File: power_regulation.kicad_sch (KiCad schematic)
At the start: 52 parts, among them J2 Conn_01x02, J3 Conn_02x01, U2 LM3880-1AA, U3 LMR33630BDDA, U4 LMR33630BDDA, U5 TPS78533QKVURQ1, U6 TPS78450QDBVRQ1

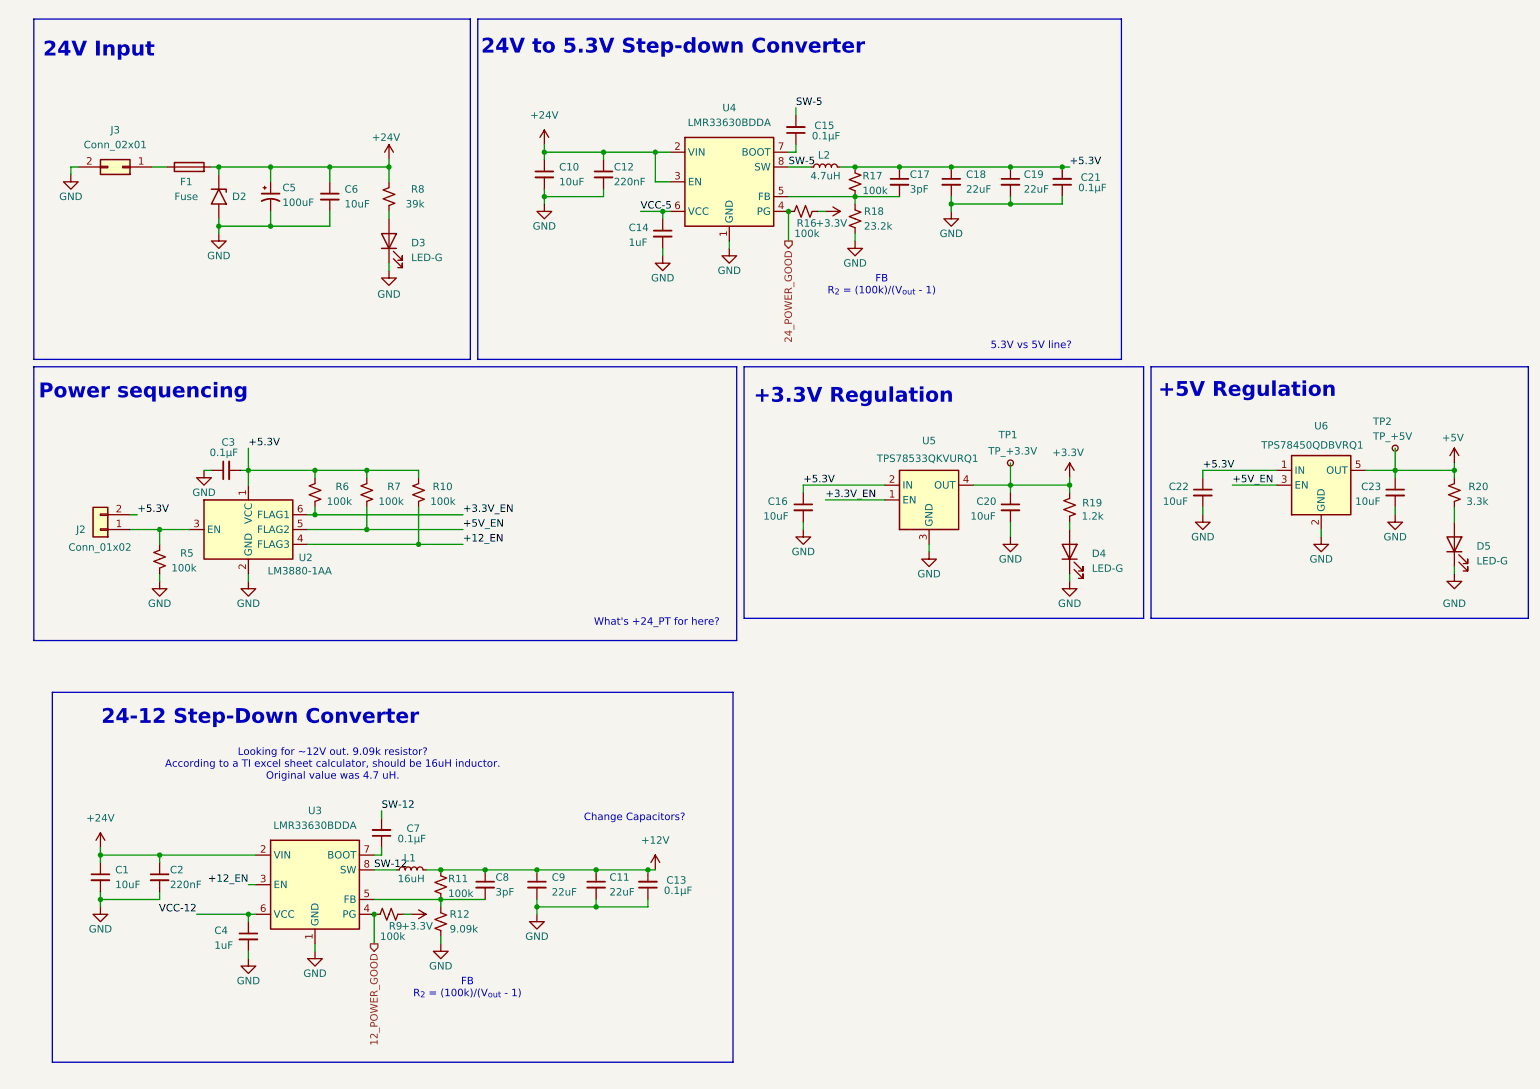
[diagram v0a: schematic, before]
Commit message: update buck converter components and add reverse polarity protection
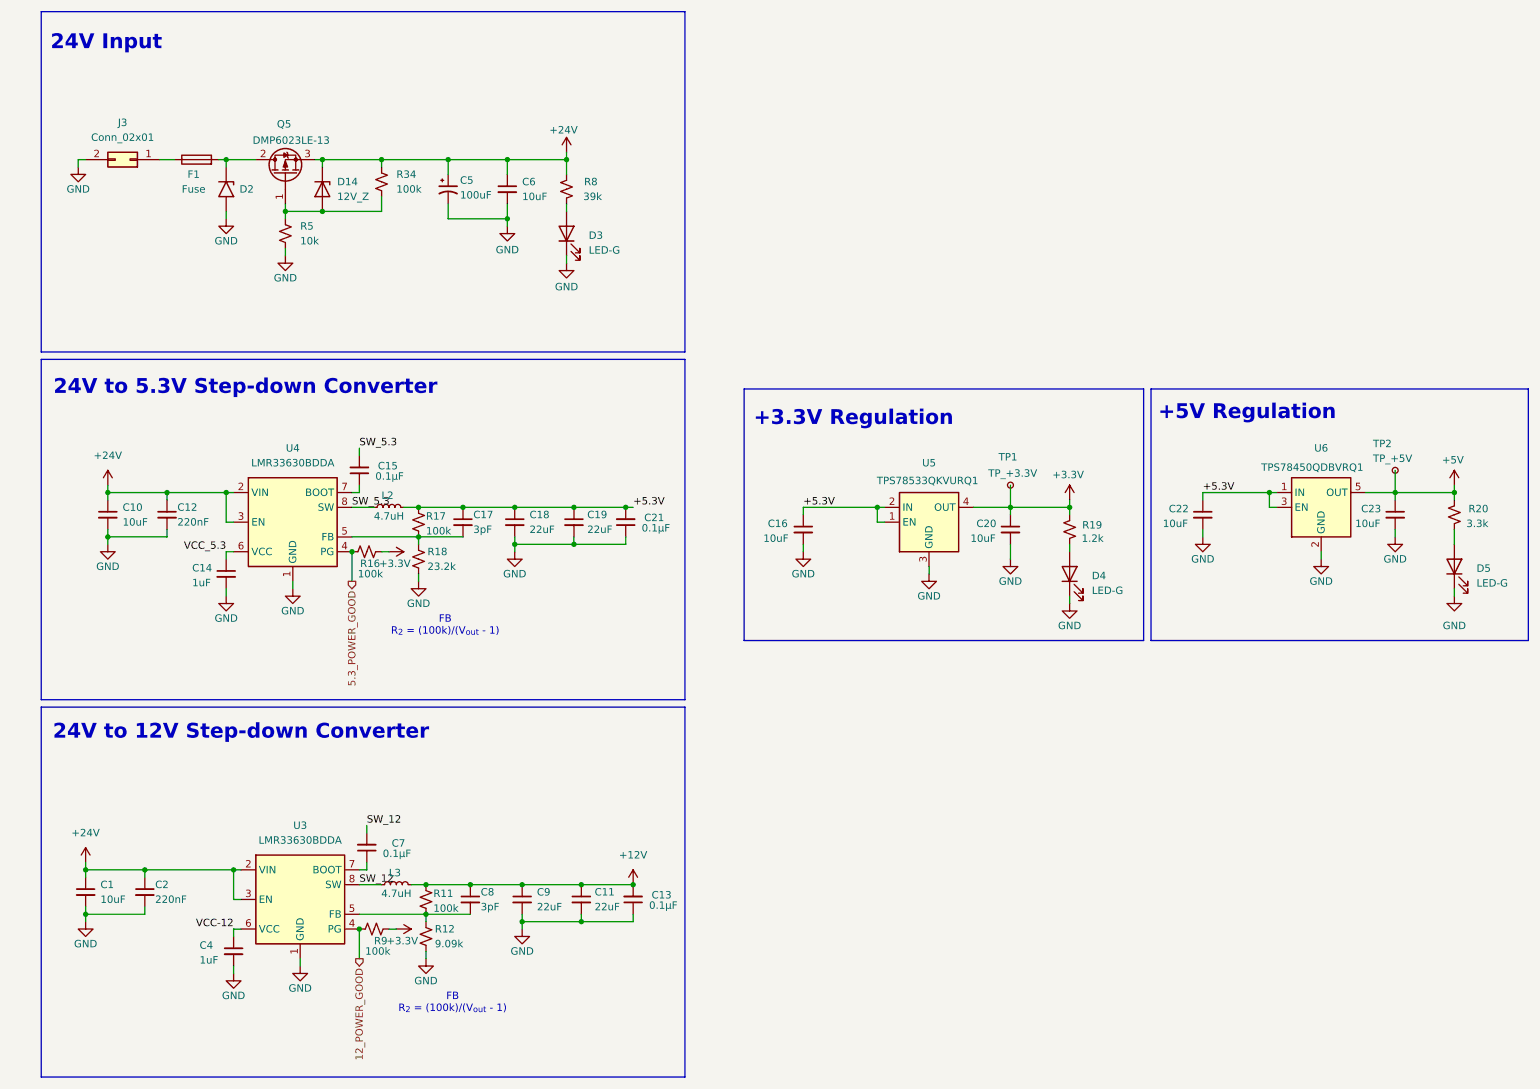
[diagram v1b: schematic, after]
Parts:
- removed C3: 0.1μF, Capacitor_SMD:C_0402_1005Metric, symbol Device:C_Small
- removed J2: Conn_01x02, Connector_Molex:Molex_Micro-Fit_3.0_43650-0215_1x02_P3.00mm_Vertical, symbol Connector_Generic:Conn_01x02
- removed L1: 16uH, Inductor_SMD:L_Bourns_SRP7028A_7.3x6.6mm, symbol Device:L_Small
- removed R10, R6, R7: 100k, Resistor_SMD:R_0603_1608Metric, symbol Device:R_Small_US
- removed U2: LM3880-1AA, Package_TO_SOT_SMD:SOT-23-6, symbol Power_Supervisor:LM3880
- added D14: 12V_Z, Diode_SMD:D_SOD-123, symbol Device:D_Zener
- added L3: 4.7uH, Inductor_SMD:L_Bourns_SRP7028A_7.3x6.6mm, symbol Device:L_Small
- added Q5: DMP6023LE-13, Package_TO_SOT_SMD:SOT-223-3_TabPin2, symbol Transistor_FET:ZXMP4A16G
- added R34: 100k, Resistor_SMD:R_0603_1608Metric, symbol Device:R_Small_US
- R12, R18: LCSC C25890 -> (none)
- R5: value 100k -> 10k
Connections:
- net +12_EN is gone; now on net +24V: U3.3 (EN)
- net +3.3V_EN is gone; now on net +5.3V: U5.1 (EN)
- net +5V_EN is gone; now on net +5.3V: U6.3 (EN)
- net +12V: now also L3.2
- net +24V: now also D14.1 (K), Q5.3 (S), R34.1; no longer D2.1 (A1), F1.2
- net GND: now also R5.2; no longer R5.1
- net 24_POWER_GOOD renamed 5.3_POWER_GOOD
- net SW-12 renamed SW_12
- net SW_12: now also L3.1
- net SW-5 renamed SW_5.3
- net VCC-5 renamed VCC_5.3
- new net: D14.2 (A), Q5.1 (G), R34.2, R5.1
- new net: D2.1 (A1), F1.2, Q5.2 (D)
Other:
- note added: "24V to 12V Step-down Converter"
- note removed: "24-12 Step-Down Converter"
- note removed: "5.3V vs 5V line?"
- note removed: "Change Capacitors?"
- note removed: "Looking for ~12V out. 9.09k resistor? According to a TI excel sheet calculator, should be 16uH inductor. Original value was 4.7 uH."
- note removed: "Power sequencing"
- note removed: "What's +24_PT for here?"
- moved on the sheet: C1, C10, C11, C12, C13, C14, C15, C16, C17, C18, C19, C2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

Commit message: do some pcb routing
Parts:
- renumbered C12 to C10, C14 to C11, C4 to C12, C15 to C13, C7 to C14, C5 to C15, C17 to C16, C8 to C17, C6 to C18, C18 to C19, C9 to C20, C19 to C21, C11 to C22, C21 to C23, C13 to C24, C16 to C25, C20 to C26, C22 to C27, C23 to C28, C1 to C7, C10 to C8, C2 to C9, D2 to D5, D14 to D6, D3 to D7, D4 to D8, D5 to D9, J3 to J4, L2 to L1, L3 to L2, Q5 to Q1, R16 to R10, R9 to R11, R34 to R12, R17 to R13, R18 to R14, R11 to R15, R12 to R16, R8 to R17, R19 to R18, R20 to R19, R5 to R9, TP1 to TP3, TP2 to TP4, U4 to U2, U5 to U4, U6 to U5
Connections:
- net VCC-12 renamed VCC_12
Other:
- moved on the sheet: C12, C14, C17, C20, C22, C24, C7, C9, L2, R11, R15, R16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

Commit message: finish pcb routing
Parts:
- added C34, C35, C36: 0.1μF, Capacitor_SMD:C_0402_1005Metric, symbol Device:C_Small
- added TP5: GND_TP, TestPoint:TestPoint_Loop_D2.50mm_Drill1.0mm, symbol Connector:TestPoint
- added TP6: 24V_TP, TestPoint:TestPoint_Loop_D2.50mm_Drill1.0mm, symbol Connector:TestPoint
- added U7: LM66200DRLR, Package_TO_SOT_SMD:SOT-583-8, symbol LM66200DRLR:LM66200DRLR
- R14: value 23.2k -> 24k
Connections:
- net +24V: now also TP6.1
- net GND: now also C34.1, C35.1, C36.1, TP5.1, U7.1 (GND), U7.4 (~{ON}), U7.5 (GND)
- net +5.3V renamed +5.17V
- net +5.17V: now also C36.2, U7.2 (VOUT), U7.7 (VOUT); no longer C16.1, C19.1, C21.1, C23.2, L1.2, R13.1
- net 5.3_POWER_GOOD renamed 5.17_POWER_GOOD
- new net +5.17V_PRE: C16.1, C19.1, C21.1, C23.2, C34.2, L1.2, R13.1, U7.3 (VIN1)
- new net 5V_USB: C35.2, U7.6 (VIN2)
- no-connect marks 0 -> 1
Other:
- note added: "24V to 5.17V Step-down Converter"
- note added: "USB ORing"
- note added: "Use buck to drop just above 5V so that ripple can be smoothed by 5V LDO"
- note removed: "24V to 5.3V Step-down Converter"

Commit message: remove unneccesary component fields
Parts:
- C10, C9: Dielectric X5R or X7R -> (none); LCSC C5378 -> (none); Voltage 50V -> (none)
- C11, C12: Dielectric X5R or X7R -> (none); LCSC C29936 -> (none)
- C13, C14, C23, C24, C34, C35, C36: value 0.1μF -> 100nF; LCSC C307331 -> (none); MPN CL05B104KO5NNNC -> (none)
- C16, C17: Dielectric X5R or X7R -> (none); LCSC C695157 -> (none)
- C18: footprint Capacitor_SMD:C_1812_4532Metric -> Capacitor_SMD:C_1206_3216Metric; Dielectric X5R or X7R -> (none); P/N CL31A106KBHNNNE -> (none); Voltage 50V -> (none)
- C19, C20, C21, C22: Dielectric X5R or X7R -> (none); LCSC C602037 -> (none)
- C25, C26, C27, C28: Dielectric X5R or X7R -> (none); LCSC C15850 -> (none)
- C7, C8: Dielectric X5R or X7R -> (none); LCSC C13585 -> (none); P/N CL31A106KBHNNNE -> (none); Voltage 50V -> (none)
- F1, J4, TP3, TP4, TP5, TP6: LCSC (none) -> N/A; now left out of the parts list
- R10, R11, R13, R15: value 100k -> 100kΩ; LCSC C25531 -> (none); MPN 0402WGJ0103TCE -> (none)
- R12: value 100k -> 100kΩ; LCSC C25530 -> (none); MPN 0402WGJ0104TCE -> (none)
- R14: value 24k -> 24kΩ; MPN 0402WGF3301TCE -> (none)
- R16: value 9.09k -> 9.09kΩ; MPN 0402WGF3301TCE -> (none)
- R17: value 39k -> 39kΩ
- R18: value 1.2k -> 1.2kΩ
- R19: value 3.3k -> 3.3kΩ
- R9: value 10k -> 10kΩ
- U7: value LM66200DRLR -> LM66200
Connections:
- net GND: no longer U4.4 (OUT), U5.4 (GND)

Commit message: add all lcsc part numbers
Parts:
- C10, C9: LCSC (none) -> C5378
- C11, C12: LCSC (none) -> C29936
- C13, C14, C23, C24, C34, C35, C36: LCSC (none) -> C85858
- C16, C17: LCSC (none) -> C162223
- C18, C7, C8: LCSC (none) -> C13585
- C19, C20, C21, C22: LCSC (none) -> C45783
- C25, C26, C27, C28: LCSC (none) -> C15850
- R10, R11, R12, R13, R15: LCSC (none) -> C122538
- R14: LCSC (none) -> C326729
- R16: LCSC (none) -> C861611
- R17: LCSC (none) -> C137995
- R18: LCSC (none) -> C138040
- R19: LCSC (none) -> C137992
- R9: LCSC (none) -> C99198
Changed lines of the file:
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@@
 			)
 		)
-		(property "LCSC" ""
+		(property "LCSC" "C5378"
 			(at 30.48 165.1 0)
 			(hide yes)
@@
 			)
 		)
-		(property "LCSC" ""
+		(property "LCSC" "C13585"
 			(at 20.32 165.1 0)
 			(hide yes)
@@
 			)
 		)
-		(property "LCSC" ""
+		(property "LCSC" "C122538"
 			(at 78.74 166.37 0)
 			(hide yes)
@@
 			)
 		)
-		(property "LCSC" ""
+		(property "LCSC" "C85858"
 			(at 181.61 43.18 0)
 			(hide yes)
@@
 			)
 		)
-		(property "LCSC" ""
+		(property "LCSC" "C122538"
 			(at 72.39 43.18 0)
 			(hide yes)
@@
 			)
 		)
-		(property "LCSC" ""
+		(property "LCSC" "C15850"
 			(at 144.78 102.87 0)
 			(hide yes)
@@
 			)
 		)
-		(property "LCSC" ""
+		(property "LCSC" "C85858"
 			(at 68.58 92.71 0)
 			(hide yes)
@@
 			)
 		)
-		(property "LCSC" ""
+		(property "LCSC" "C861611"
 			(at 78.74 172.72 0)
 			(hide yes)
@@
 			)
 		)
-		(property "LCSC" ""
+		(property "LCSC" "C5378"
 			(at 35.56 100.33 0)
 			(hide yes)
@@
 			)
 		)
-		(property "LCSC" ""
+		(property "LCSC" "C45783"
 			(at 95.25 166.37 0)
 			(hide yes)
@@
 			)
 		)
-		(property "LCSC" ""
+		(property "LCSC" "C15850"
 			(at 180.34 102.87 0)
 			(hide yes)
@@
 			)
 		)
-		(property "LCSC" ""
+		(property "LCSC" "C29936"
 			(at 45.72 110.49 0)
 			(hide yes)
@@
 			)
 		)
-		(property "LCSC" ""
+		(property "LCSC" "C13585"
 			(at 25.4 100.33 0)
 			(hide yes)
@@
 			)
 		)
-		(property "LCSC" ""
+		(property "LCSC" "C326729"
 			(at 78.74 107.95 0)
 			(hide yes)
@@
 			)
 		)
-		(property "LCSC" ""
+		(property "LCSC" "C29936"
 			(at 45.72 175.26 0)
 			(hide yes)
@@
 			)
 		)
-		(property "LCSC" ""
+		(property "LCSC" "C85858"
 			(at 114.3 101.6 0)
 			(hide yes)
@@
 			)
 		)
-		(property "LCSC" ""
+		(property "LCSC" "C45783"
 			(at 105.41 166.37 0)
 			(hide yes)
@@
 			)
 		)
-		(property "LCSC" ""
+		(property "LCSC" "C15850"
 			(at 246.38 100.33 0)
 			(hide yes)
@@
 			)
 		)
-		(property "LCSC" ""
+		(property "LCSC" "C162223"
 			(at 86.36 101.6 0)
 			(hide yes)
@@
 			)
 		)
-		(property "LCSC" ""
+		(property "LCSC" "C15850"
 			(at 213.36 100.33 0)
 			(hide yes)
@@
 			)
 		)
-		(property "LCSC" ""
+		(property "LCSC" "C85858"
 			(at 185.42 55.88 0)
 			(hide yes)
@@
 			)
 		)
+		(property "LCSC" "C137992"
+			(at 256.54 100.33 0)
+			(hide yes)
+			(show_name no)
+			(do_not_autoplace no)
+			(effects
+				(font
+					(size 1.27 1.27)
+				)
+			)
+		)
 		(pin "2"
 		)
@@
 			)
 		)
+		(property "LCSC" "C137995"
+			(at 104.14 44.45 0)
+			(hide yes)
+			(show_name no)
+			(do_not_autoplace no)
+			(effects
+				(font
+					(size 1.27 1.27)
+				)
+			)
+		)
 		(pin "2"
 		)
@@
 			)
 		)
-		(property "LCSC" ""
+		(property "LCSC" "C85858"
 			(at 68.58 157.48 0)
 			(hide yes)
@@
 			)
 		)
-		(property "LCSC" ""
+		(property "LCSC" "C45783"
 			(at 105.41 101.6 0)
 			(hide yes)
@@
 			)
 		)
-		(property "LCSC" ""
+		(property "LCSC" "C122538"
 			(at 69.85 171.45 0)
 			(hide yes)
@@
 			)
 		)
-		(property "LCSC" ""
+		(property "LCSC" "C99198"
 			(at 55.88 52.07 0)
 			(hide yes)
@@
 			)
 		)
-		(property "LCSC" ""
+		(property "LCSC" "C122538"
 			(at 78.74 101.6 0)
 			(hide yes)
@@
 			)
 		)
-		(property "LCSC" ""
+		(property "LCSC" "C85858"
 			(at 220.98 44.45 0)
 			(hide yes)
@@
 			)
 		)
-		(property "LCSC" ""
+		(property "LCSC" "C45783"
 			(at 95.25 101.6 0)
 			(hide yes)
@@
 			)
 		)
-		(property "LCSC" ""
+		(property "LCSC" "C13585"
 			(at 93.98 44.45 0)
 			(hide yes)
@@
 			)
 		)
-		(property "LCSC" ""
+		(property "LCSC" "C122538"
 			(at 69.85 106.68 0)
 			(hide yes)
@@
 			)
 		)
-		(property "LCSC" ""
+		(property "LCSC" "C162223"
 			(at 86.36 166.37 0)
 			(hide yes)
@@
 			)
 		)
+		(property "LCSC" "C138040"
+			(at 190.5 102.87 0)
+			(hide yes)
+			(show_name no)
+			(do_not_autoplace no)
+			(effects
+				(font
+					(size 1.27 1.27)
+				)
+			)
+		)
 		(pin "2"
 		)
@@
 			)
 		)
-		(property "LCSC" ""
+		(property "LCSC" "C85858"
 			(at 114.3 166.37 0)
 			(hide yes)

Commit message: fix 5.17V buck switch node net name
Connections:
- net SW_5.3 renamed SW_5.17
- net VCC_5.3 renamed VCC_5.17
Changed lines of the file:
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@@
 		)
 	)
-	(label "SW_5.3"
+	(label "SW_5.17"
 		(at 68.58 88.9 0)
 		(effects
@@
 		)
 	)
-	(label "VCC_5.3"
+	(label "VCC_5.17"
 		(at 45.72 106.68 180)
 		(effects
@@
 		)
 	)
-	(label "SW_5.3"
+	(label "SW_5.17"
 		(at 67.31 99.06 0)
 		(effects

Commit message: update all capacitors to jlcpcb basic components
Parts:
- C11, C12: LCSC C29936 -> C15849
- C13, C14, C23, C24, C34, C35, C36: LCSC C85858 -> C307331
- C16, C17: value 3pF -> 10pF; LCSC C162223 -> C1634
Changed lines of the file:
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@@
 			)
 		)
-		(property "LCSC" "C85858"
+		(property "LCSC" "C307331"
 			(at 181.61 43.18 0)
 			(hide yes)
@@
 			)
 		)
-		(property "LCSC" "C85858"
+		(property "LCSC" "C307331"
 			(at 68.58 92.71 0)
 			(hide yes)
@@
 			)
 		)
-		(property "LCSC" "C29936"
+		(property "LCSC" "C15849"
 			(at 45.72 110.49 0)
 			(hide yes)
@@
 			)
 		)
-		(property "LCSC" "C29936"
+		(property "LCSC" "C15849"
 			(at 45.72 175.26 0)
 			(hide yes)
@@
 			)
 		)
-		(property "LCSC" "C85858"
+		(property "LCSC" "C307331"
 			(at 114.3 101.6 0)
 			(hide yes)
@@
 			)
 		)
-		(property "Value" "3pF"
+		(property "Value" "10pF"
 			(at 88.138 102.87 0)
 			(show_name no)
@@
 			)
 		)
-		(property "LCSC" "C162223"
+		(property "LCSC" "C1634"
 			(at 86.36 101.6 0)
 			(hide yes)
@@
 			)
 		)
-		(property "LCSC" "C85858"
+		(property "LCSC" "C307331"
 			(at 185.42 55.88 0)
 			(hide yes)
@@
 			)
 		)
-		(property "LCSC" "C85858"
+		(property "LCSC" "C307331"
 			(at 68.58 157.48 0)
 			(hide yes)
@@
 			)
 		)
-		(property "LCSC" "C85858"
+		(property "LCSC" "C307331"
 			(at 220.98 44.45 0)
 			(hide yes)
@@
 			)
 		)
-		(property "Value" "3pF"
+		(property "Value" "10pF"
 			(at 88.138 167.64 0)
 			(show_name no)
@@
 			)
 		)
-		(property "LCSC" "C162223"
+		(property "LCSC" "C1634"
 			(at 86.36 166.37 0)
 			(hide yes)
@@
 			)
 		)
-		(property "LCSC" "C85858"
+		(property "LCSC" "C307331"
 			(at 114.3 166.37 0)
 			(hide yes)

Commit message: add a 12v testpoint
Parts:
- added TP7: TP_+12V, TestPoint:TestPoint_Pad_D1.0mm, symbol Connector:TestPoint_Small
- R10, R11, R12, R13, R15: LCSC C122538 -> (none)
- R14: LCSC C326729 -> (none)
- R16: LCSC C861611 -> (none)
- R17: LCSC C137995 -> (none)
- R18: LCSC C138040 -> (none)
- R19: LCSC C137992 -> (none)
- R9: LCSC C99198 -> (none)
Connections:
- net +12V: now also TP7.1
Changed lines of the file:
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@@
 	(wire
 		(pts
+			(xy 105.41 160.02) (xy 105.41 163.83)
+		)
+		(stroke
+			(width 0)
+			(type default)
+		)
+	)
+	(wire
+		(pts
 			(xy 200.66 55.88) (xy 201.93 55.88)
 		)
@@
 			)
 		)
-		(property "LCSC" "C122538"
+		(property "LCSC" ""
 			(at 78.74 166.37 0)
 			(hide yes)
@@
 			)
 		)
-		(property "LCSC" "C122538"
+		(property "LCSC" ""
 			(at 72.39 43.18 0)
 			(hide yes)
@@
 			)
 		)
-		(property "LCSC" "C861611"
+		(property "LCSC" ""
 			(at 78.74 172.72 0)
 			(hide yes)
@@
 			)
 		)
-		(property "LCSC" "C326729"
+		(property "LCSC" ""
 			(at 78.74 107.95 0)
 			(hide yes)
@@
 	)
 	(symbol
+		(lib_id "Connector:TestPoint_Small")
+		(at 105.41 160.02 0)
+		(unit 1)
+		(body_style 1)
+		(exclude_from_sim no)
+		(in_bom no)
+		(on_board yes)
+		(in_pos_files no)
+		(dnp no)
+		(property "Reference" "TP7"
+			(at 103.378 155.194 0)
+			(show_name no)
+			(do_not_autoplace no)
+			(effects
+				(font
+					(size 1.27 1.27)
+				)
+				(justify left)
+			)
+		)
+		(property "Value" "TP_+12V"
+			(at 101.6 157.988 0)
+			(show_name no)
+			(do_not_autoplace no)
+			(effects
+				(font
+					(size 1.27 1.27)
+				)
+				(justify left)
+			)
+		)
+		(property "Footprint" "TestPoint:TestPoint_Pad_D1.0mm"
+			(at 110.49 160.02 0)
+			(hide yes)
+			(show_name no)
+			(do_not_autoplace no)
+			(effects
+				(font
+					(size 1.27 1.27)
+				)
+			)
+		)
+		(property "Datasheet" ""
+			(at 110.49 160.02 0)
+			(hide yes)
+			(show_name no)
+			(do_not_autoplace no)
+			(effects
+				(font
+					(size 1.27 1.27)
+				)
+			)
+		)
+		(property "Description" "test point"
+			(at 105.41 160.02 0)
+			(hide yes)
+			(show_name no)
+			(do_not_autoplace no)
+			(effects
+				(font
+					(size 1.27 1.27)
+				)
+			)
+		)
+		(property "LCSC" "N/A"
+			(at 105.41 160.02 0)
+			(hide yes)
+			(show_name no)
+			(do_not_autoplace no)
+			(effects
+				(font
+					(size 1.27 1.27)
+				)
+			)
+		)
+		(pin "1"
+		)
+		(instances
+			(project "gse_control_node"
+				(path "/24817451-dfe0-4b9a-9d93-7304529c9d58/ee31919e-6383-4dab-aec3-a18ec94a437b"
+					(reference "TP7")
+					(unit 1)
+				)
+			)
+		)
+	)
+	(symbol
 		(lib_id "Device:C_Small")
 		(at 185.42 55.88 180)
@@
 			)
 		)
-		(property "LCSC" "C137992"
+		(property "LCSC" ""
 			(at 256.54 100.33 0)
 			(hide yes)
@@
 			)
 		)
-		(property "LCSC" "C137995"
+		(property "LCSC" ""
 			(at 104.14 44.45 0)
 			(hide yes)
@@
 			)
 		)
-		(property "LCSC" "C122538"
+		(property "LCSC" ""
 			(at 69.85 171.45 0)
 			(hide yes)
@@
 			)
 		)
-		(property "LCSC" "C99198"
+		(property "LCSC" ""
 			(at 55.88 52.07 0)
 			(hide yes)
@@
 			)
 		)
-		(property "LCSC" "C122538"
+		(property "LCSC" ""
 			(at 78.74 101.6 0)
 			(hide yes)
@@
 			)
 		)
-		(property "LCSC" "C122538"
+		(property "LCSC" ""
 			(at 69.85 106.68 0)
 			(hide yes)
@@
 			)
 		)
-		(property "LCSC" "C138040"
+		(property "LCSC" ""
 			(at 190.5 102.87 0)
 			(hide yes)
